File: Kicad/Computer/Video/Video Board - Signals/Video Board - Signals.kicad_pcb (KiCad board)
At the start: 2 copper layers, 248.9 x 161.9 mm, 41 parts, among them IC1 LD1117S50C, IC2 SST39VF010-70-4I-NHE, IC3 74LVC573APW,118, J1 Conn_01x08_Pin, J2 Conn_01x40_Pin, J3 Conn_01x40_Pin, J4 Conn_01x40_Pin, J5 395-098-520-350, J6 Conn_01x08_Pin

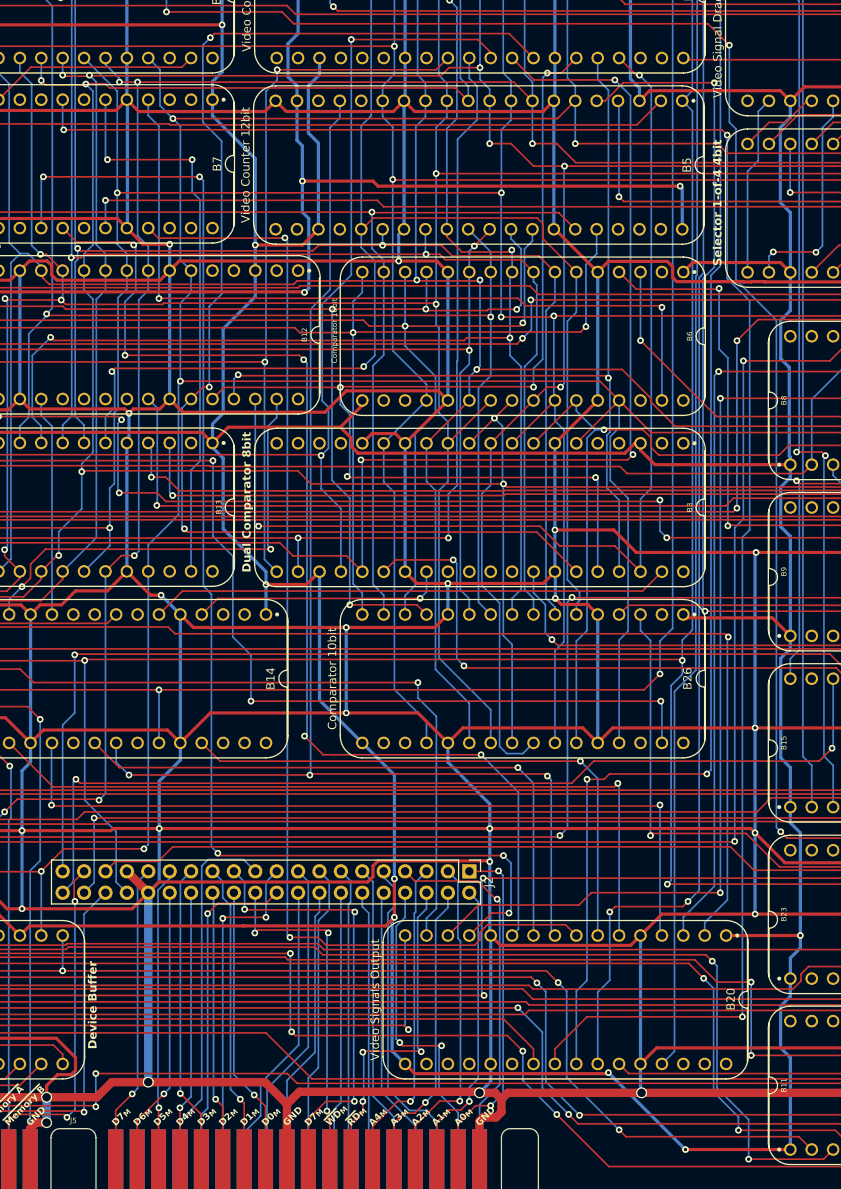
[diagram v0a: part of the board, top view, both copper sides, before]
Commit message: Forgot to clean up traces.  Regenerated video board Gerbers.
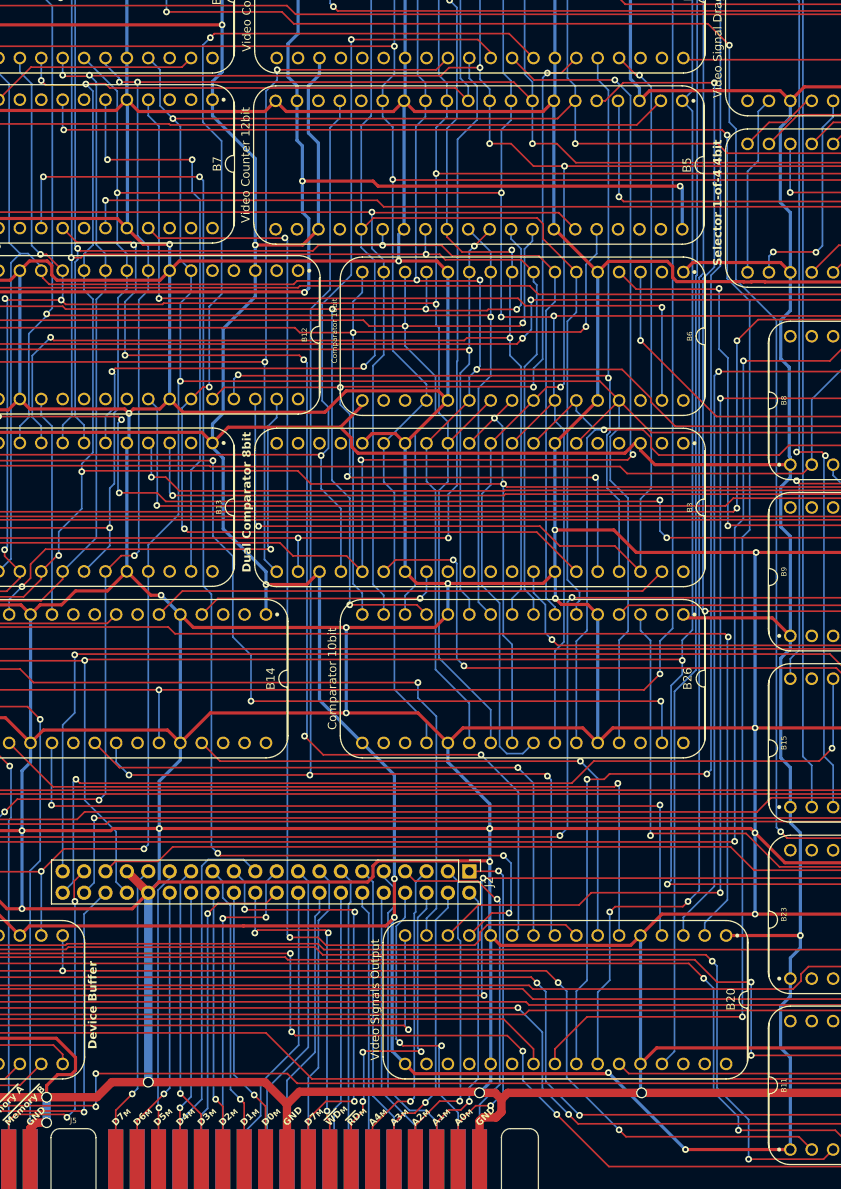
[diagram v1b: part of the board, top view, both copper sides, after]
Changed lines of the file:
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@@
 		(fp_arc
 			(start 86.040048 -8.4)
-			(mid 86.357626 -9.156454)
+			(mid 86.35762 -9.156489)
 			(end 87.117096 -9.466799)
 			(stroke
@@
 		(fp_arc
 			(start 90.297 -9.466799)
-			(mid 91.056476 -9.156459)
+			(mid 91.056441 -9.156453)
 			(end 91.374048 -8.4)
 			(stroke
@@
 		(fp_arc
 			(start 139.499048 -8.4)
-			(mid 139.816626 -9.156454)
+			(mid 139.81662 -9.156489)
 			(end 140.576096 -9.466799)
 			(stroke
@@
 		(fp_arc
 			(start 14.404267 -2.613733)
-			(mid 16.252448 -1.848183)
+			(mid 16.252451 -1.848184)
 			(end 17.017999 -0.000001)
 			(stroke
@@
 		(fp_arc
 			(start 14.404267 -2.613733)
-			(mid 16.252448 -1.848183)
+			(mid 16.252451 -1.848184)
 			(end 17.017999 -0.000001)
 			(stroke
@@
 		(fp_arc
 			(start 14.404267 -2.613733)
-			(mid 16.252451 -1.848184)
+			(mid 16.252448 -1.848183)
 			(end 17.017999 -0.000001)
 			(stroke
@@
 		(fp_arc
 			(start 14.404267 -2.613733)
-			(mid 16.252448 -1.848183)
+			(mid 16.252451 -1.848184)
 			(end 17.017999 -0.000001)
 			(stroke
@@
 		(fp_arc
 			(start 24.763183 0.179239)
-			(mid 25.272985 -1.051589)
+			(mid 25.272978 -1.051587)
 			(end 26.503802 -1.56138)
 			(stroke
@@
 		(fp_arc
 			(start 14.404267 -2.613733)
-			(mid 16.252448 -1.848183)
+			(mid 16.252451 -1.848184)
 			(end 17.017999 -0.000001)
 			(stroke
@@
 		(fp_arc
 			(start 14.404267 -2.613733)
-			(mid 16.252448 -1.848183)
+			(mid 16.252451 -1.848184)
 			(end 17.017999 -0.000001)
 			(stroke
@@
 		(fp_arc
 			(start 14.404267 -2.613733)
-			(mid 16.252448 -1.848183)
+			(mid 16.252451 -1.848184)
 			(end 17.017999 -0.000001)
 			(stroke
@@
 		(fp_arc
 			(start 14.404267 -2.613733)
-			(mid 16.252448 -1.848183)
+			(mid 16.252451 -1.848184)
 			(end 17.017999 -0.000001)
 			(stroke

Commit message: Realised I haven't committed in ages.  Oops.
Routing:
- net /GND: vias 91 -> 89
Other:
- board text added: "A0"
- board text added: "A0M"
- board text added: "A1"
- board text added: "A10"
- board text added: "A10M"
- board text added: "A11"
- board text added: "A11M"
- board text added: "A12"
- board text added: "A12M"
- board text added: "A13"
- board text added: "A13M"
- board text added: "A14"
- board text added: "A14M"
- board text added: "A15"
- board text added: "A15M"
- board text added: "A16"
- board text added: "A16M"
- board text added: "A17M"
- board text added: "A18M"
- board text added: "A19M"
- board text added: "A1M"
- board text added: "A2"
- board text added: "A20M"
- board text added: "A2M"
- board text added: "A3"
- board text added: "A3M"
- board text added: "A4"
- board text added: "A4M"
- board text added: "A5"
- board text added: "A5M"
- board text added: "A6"
- board text added: "A6M"
- board text added: "A7"
- board text added: "A7M"
- board text added: "A8"
- board text added: "A8M"
- board text added: "A9"
- board text added: "A9M"
- board text added: "AP"
- board text added: "B0"
- board text added: "B1"
- board text added: "B2"
- board text added: "B3"
- board text added: "B4"
- board text added: "B5"
- board text added: "B6"
- board text added: "B7"
- board text added: "CLK0"
- board text added: "CLK1"
- board text added: "CLK2"
- board text added: "CLK3"
- board text added: "D0"
- board text added: "D0M"
- board text added: "D1"
- board text added: "D1M"
- board text added: "D2"
- board text added: "D2M"
- board text added: "D3"
- board text added: "D3M"
- board text added: "D4"
- board text added: "D4M"
- board text added: "D5"
- board text added: "D5M"
- board text added: "D6"
- board text added: "D6M"
- board text added: "D7"
- board text added: "D7M"
- board text added: "G0"
- board text added: "G1"
- board text added: "G2"
- board text added: "G3"
- board text added: "G4"
- board text added: "G5"
- board text added: "G6"
- board text added: "G7"
- board text added: "HCP65 Daughter Board Video Device Signals V0"
- board text added: "LP+1"
- board text added: "Memory Frame"
- board text added: "PL0"
- board text added: "PL1"
- board text added: "PL2"
- board text added: "PL3"
- board text added: "PL4"
- board text added: "PL5"
- board text added: "PL6"
- board text added: "PL7"
- board text added: "PalW"
- board text added: "R0"
- board text added: "R1"
- board text added: "R2"
- board text added: "R3"
- board text added: "R4"
- board text added: "R5"
- board text added: "R6"
- board text added: "R7"
- board text added: "RAB"
- board text added: "RAH"
- board text added: "RAL"
- board text added: "Row1"
- board text added: "Row3"
- board text added: "Row5"
- board text added: "Row7"
- board text added: "Row9"
- board text added: "r4"
- board text added: "rw0"
- board text added: "rw2"
- board text added: "rw6"
- board text added: "rw8"
- board text added: "~{CLK0}"
- board text added: "~{CLK1}"
- board text added: "~{CLK2}"
- board text added: "~{RAM}"
- board text added: "~{RD}"
- board text added: "~{RD}M"
- board text added: "~{WD}"
- board text added: "~{WD}M"
- board text removed: "HCP65 Daughter Board Video Signals V0"

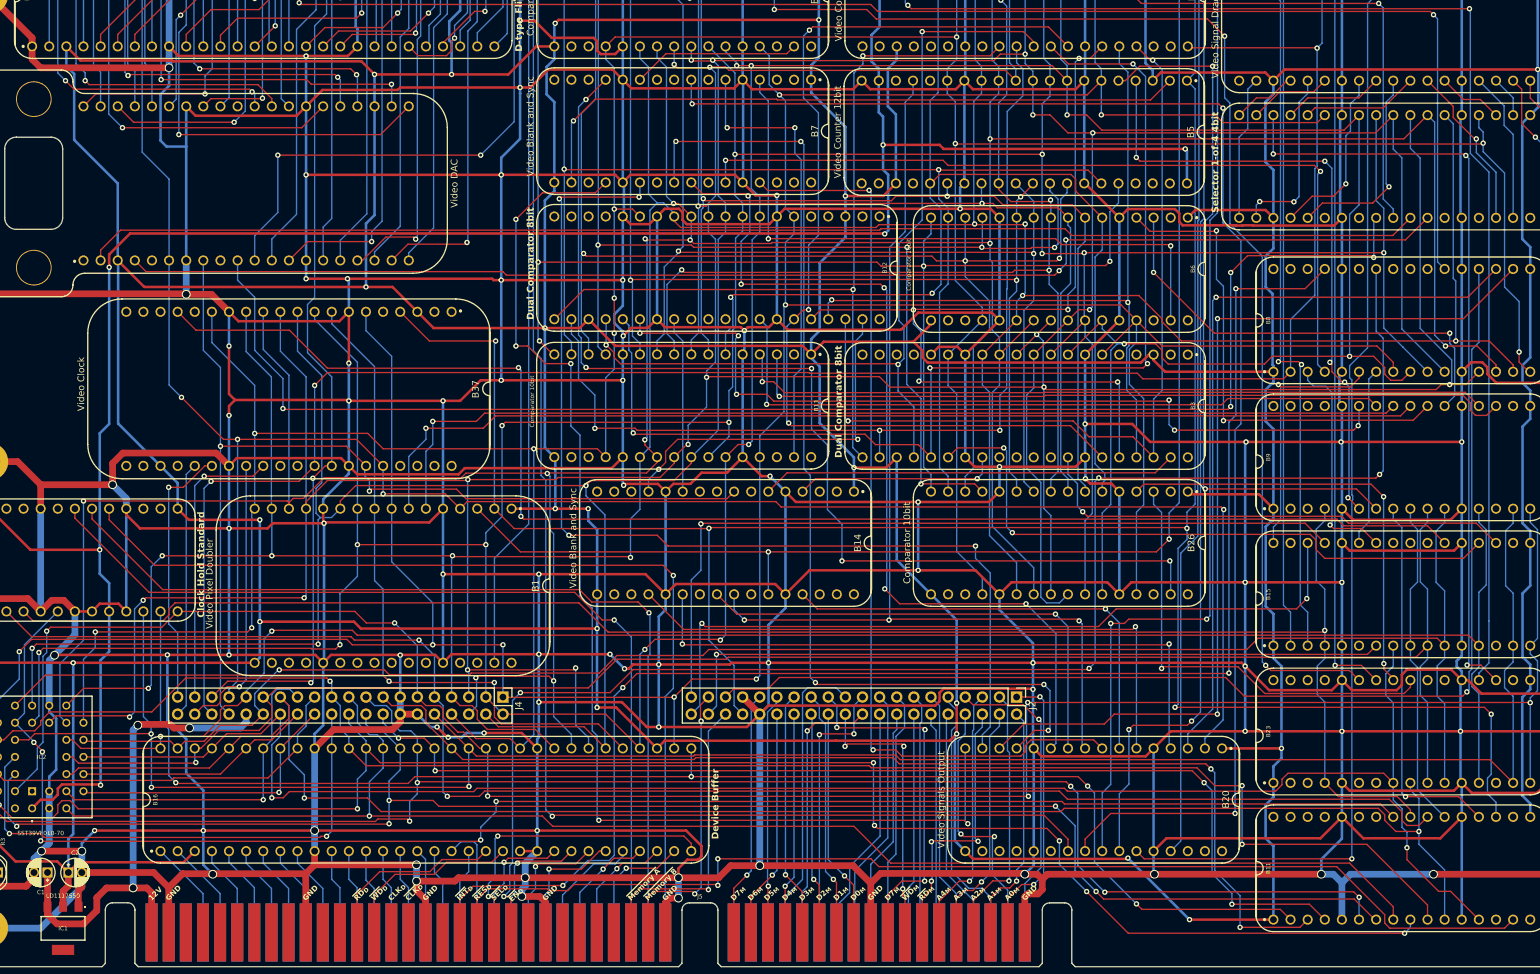
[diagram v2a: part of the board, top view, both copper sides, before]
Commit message: Started adding Graphics Board.
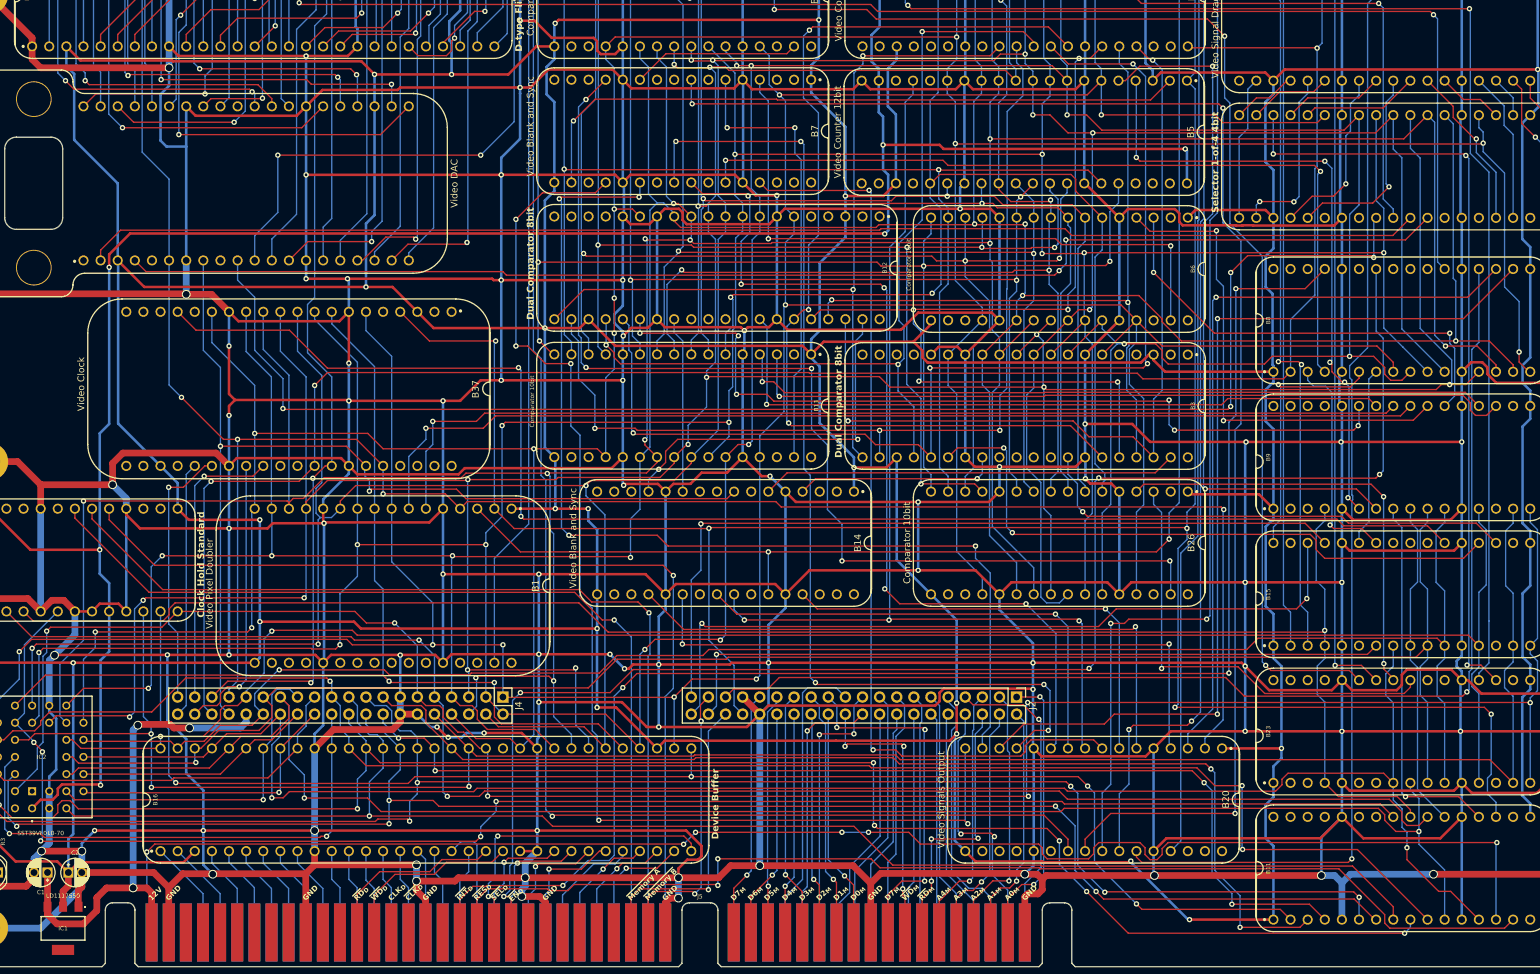
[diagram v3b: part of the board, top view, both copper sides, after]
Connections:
- B11 pad 14: unconnected-(B11-N.C.-Pad14) -> /~{Reset}_{System}
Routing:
- net /~{Reset}_{System}: track 0.00 -> 232.1 mm, vias 0 -> 6
- net /Horizontal Blank _{HALF CYCLE}: track 166.0 -> 167.0 mm
- net /A10: track 241.6 -> 240.8 mm

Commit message: Tidied and re-routed the Video Boards
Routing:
- net /First Pixel _{HALF CYCLE}: track 214.3 -> 173.3 mm, vias 3 -> 2
- net /D6: track 558.7 -> 599.4 mm, vias 10 -> 11
- net /Read Vertical High: track 93.7 -> 98.6 mm, vias 5 -> 2
- net /GND: track 4208.1 -> 4212.2 mm
- net /Write Vertical Back Porch Start High: track 198.2 -> 201.3 mm
- net /D7: track 574.8 -> 577.9 mm, vias 9 -> 8
- net /Read Horizontal Low: track 128.9 -> 131.9 mm, vias 4 -> 3
- net /~{Vertical Back Porch End}: track 100.3 -> 103.3 mm, vias 1 -> 2
- net /H5: track 132.7 -> 135.6 mm, vias 3 -> 2
- net /Row9: track 206.9 -> 209.6 mm
- net /3.3V: track 329.4 -> 332.1 mm
- net /Pixel CLK_{0}: track 322.4 -> 324.7 mm
- net /H7: track 150.4 -> 152.7 mm, vias 3 -> 4
- net /Read Vertical Low: track 104.8 -> 103.0 mm
- net /Write Horiztonal Sync Start: track 72.2 -> 74.0 mm
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
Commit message: Use VRML instead of STEP for Video Board.
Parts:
- moved B1 166.9 mm to (53.4, -62.9)
- moved B37 166.9 mm to (44.5, -92.1)
- moved B5 166.9 mm to (153.6, -126.4)
- moved C2 166.9 mm to (-12.4, -8.89)
- moved J2 166.9 mm to (128.3, -34.9)
- moved LED1 166.9 mm to (-22.8, -8.89)
- moved B20 166.9 mm to (158.8, -27.3)
- moved IC1 166.9 mm to (-13.1, -0.61)
- moved IC3 166.9 mm to (112.3, -152.4)
- moved J1 166.9 mm to (102.9, -154.3)
- moved J3 166.9 mm to (69.9, -154.3)
- moved B10 166.9 mm to (-24.1, -47.6)
- moved B11 166.9 mm to (166.4, -1.91)
- moved B12 166.9 mm to (108.0, -106.2)
- moved B13 166.9 mm to (97.8, -85.8)
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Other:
- outline, holes or cut-outs redrawn
